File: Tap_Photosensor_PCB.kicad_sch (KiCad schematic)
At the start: 9 parts, among them J1 Conn_01x03, U1 L78L05_SOT89, U3 ITR9608

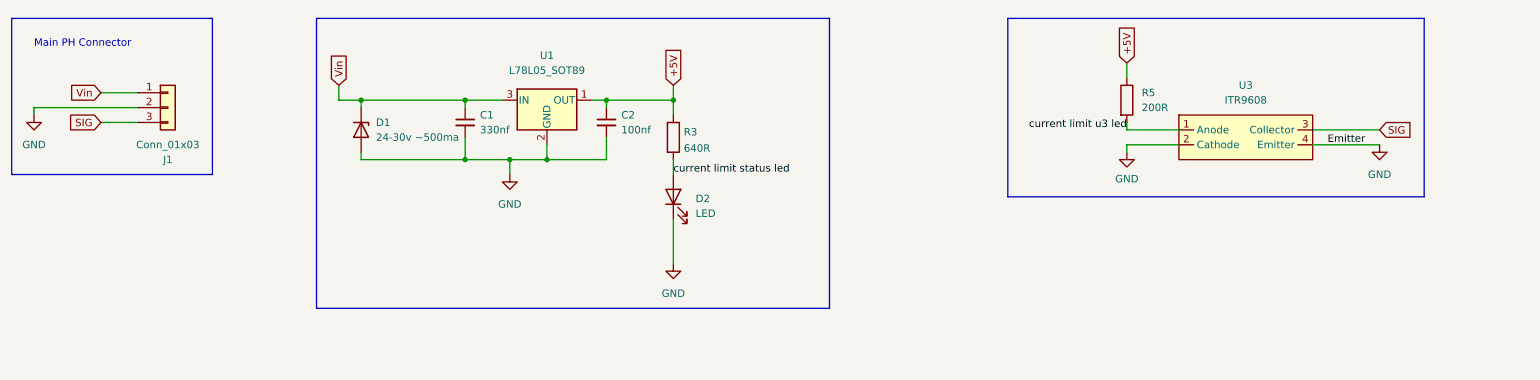
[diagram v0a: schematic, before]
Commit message: Adding panelization and R3
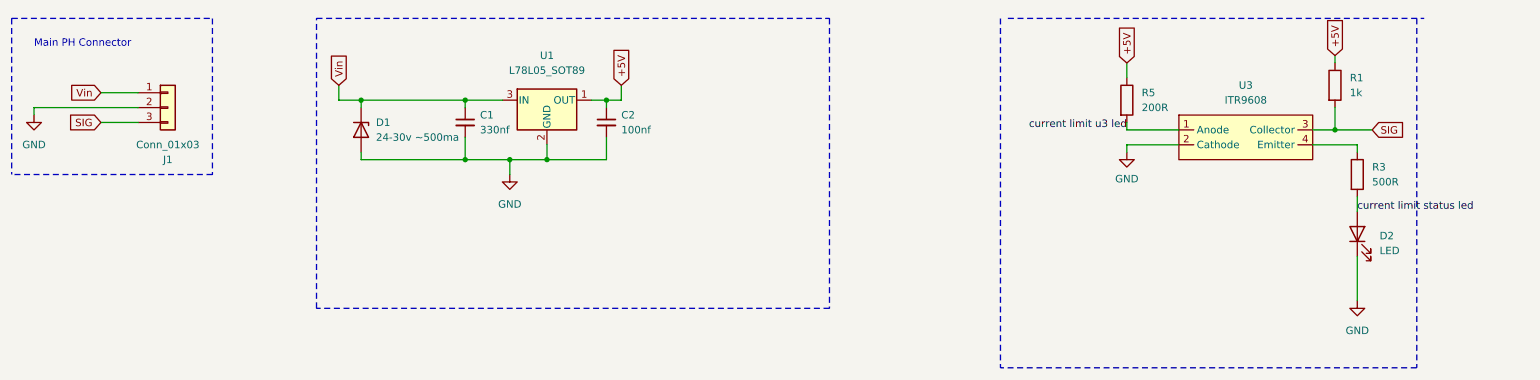
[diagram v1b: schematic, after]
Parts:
- added R1: 1k, Resistor_SMD:R_0603_1608Metric, symbol Device:R
- R3: value 640R -> 500R
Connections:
- net +5V: now also R1.1; no longer R3.1
- net GND: no longer U3.4 (Emitter)
- net SIG: now also R1.2
- new net: R3.1, U3.4 (Emitter)
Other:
- moved on the sheet: D2, R3

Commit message: fixing mistake
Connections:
- net SIG: now also R3.1, U3.4 (Emitter); no longer R1.2, U3.3 (Collector)
- new net: R1.2, U3.3 (Collector)
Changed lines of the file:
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@@
-	)
-	(junction
-		(at 264.16 41.91)
-		(diameter 0)
-		(color 0 0 0 0)
 	)
 	(junction
@@
 	(wire
 		(pts
-			(xy 264.16 41.91) (xy 270.51 41.91)
-		)
-		(stroke
-			(width 0)
-			(type default)
-		)
-	)
-	(wire
-		(pts
 			(xy 129.54 46.99) (xy 139.7 46.99)
 		)
@@
 		)
 	)
-	(global_label "+5V"
-		(shape input)
-		(at 228.6 30.48 90)
+	(global_label "SIG"
+		(shape input)
+		(at 267.97 44.45 0)
 		(fields_autoplaced yes)
 		(effects
@@
 		)
 		(property "Intersheetrefs" "${INTERSHEET_REFS}"
-			(at 228.5206 24.1964 90)
+			(at 273.4674 44.3706 0)
 			(effects
 				(font
@@
 	(global_label "+5V"
 		(shape input)
-		(at 142.24 34.29 90)
+		(at 228.6 30.48 90)
 		(fields_autoplaced yes)
 		(effects
@@
 		)
 		(property "Intersheetrefs" "${INTERSHEET_REFS}"
-			(at 142.1606 28.0064 90)
+			(at 228.5206 24.1964 90)
 			(effects
 				(font
@@
 		)
 	)
+	(global_label "+5V"
+		(shape input)
+		(at 142.24 34.29 90)
+		(fields_autoplaced yes)
+		(effects
+			(font
+				(size 1.27 1.27)
+			)
+			(justify left)
+		)
+		(property "Intersheetrefs" "${INTERSHEET_REFS}"
+			(at 142.1606 28.0064 90)
+			(effects
+				(font
+					(size 1.27 1.27)
+				)
+				(justify left)
+				(hide yes)
+			)
+		)
+	)
 	(global_label "Vin"
 		(shape input)
@@
 			(effects
 				(font
-					(size 1.27 1.27)
-				)
-				(justify left)
-				(hide yes)
-			)
-		)
-	)
-	(global_label "SIG"
-		(shape input)
-		(at 270.51 41.91 0)
-		(fields_autoplaced yes)
-		(effects
-			(font
-				(size 1.27 1.27)
-			)
-			(justify left)
-		)
-		(property "Intersheetrefs" "${INTERSHEET_REFS}"
-			(at 276.0074 41.8306 0)
-			(effects
-				(font
